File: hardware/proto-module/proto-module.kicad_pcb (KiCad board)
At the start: 2 copper layers, 80.4 x 50 mm, 4 parts, among them J1 Conn_01x30, U1 02x15_PIN_HEADER_SOCKET

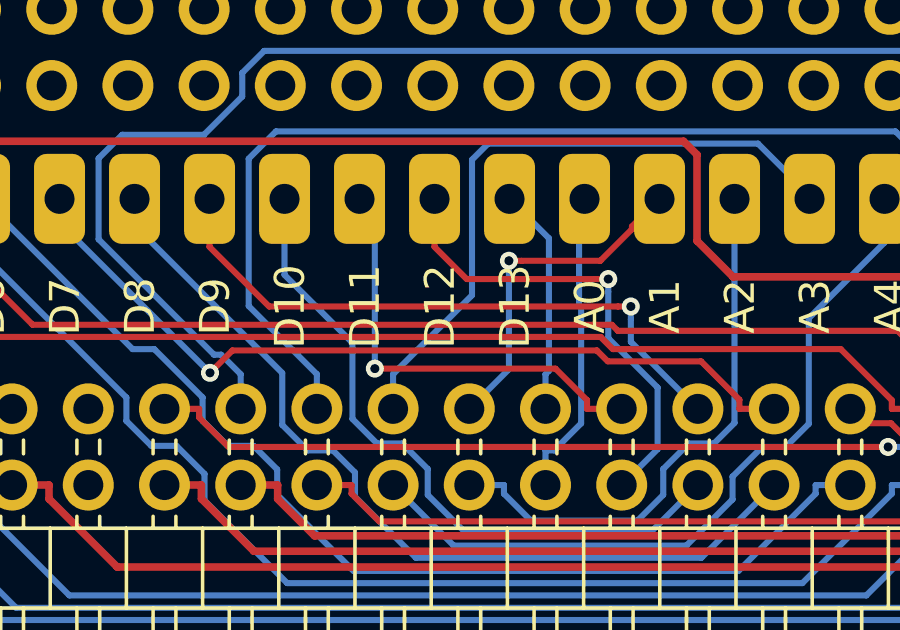
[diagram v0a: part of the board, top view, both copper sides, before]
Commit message: [hw] Make Proto Module production ready
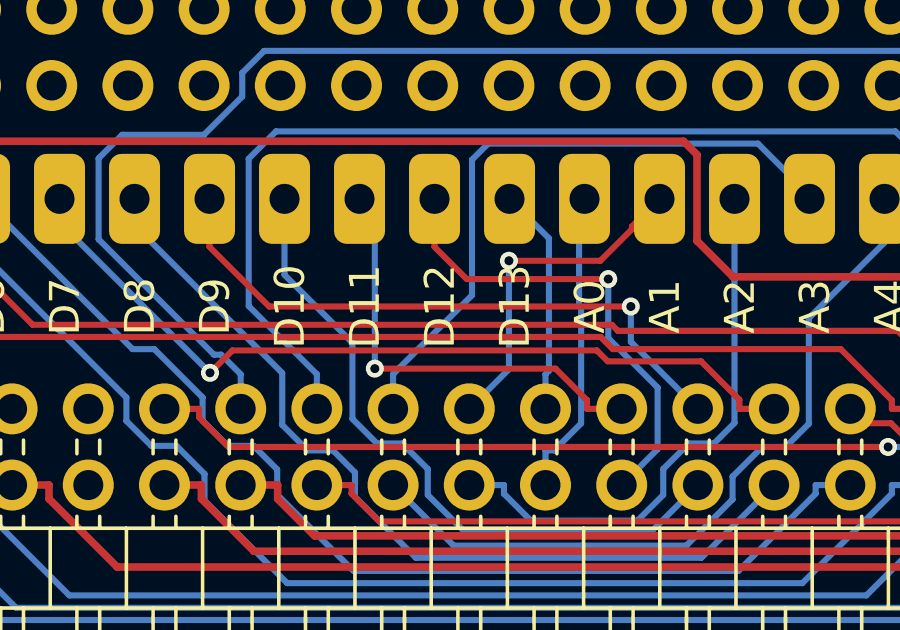
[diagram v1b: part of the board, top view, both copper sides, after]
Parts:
- moved G*** 0.69 mm to (164.9, 143.5)
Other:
- board text added: "Proto Module v0.1 : Designed by Aravinth www.arabeat.aravinth.info"
- board text removed: "Proto Module : Designed by Aravinth www.arabeat.aravinth.info"

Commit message: [hw] Make Proto Module production ready
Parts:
- moved G*** 0.31 mm to (165.1, 143.7)
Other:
- board text added: "PROTO Module v0.1 : Designed by Aravinth www.arabeat.aravinth.info"
- board text removed: "Proto Module v0.1 : Designed by Aravinth www.arabeat.aravinth.info"
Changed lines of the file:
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@@
   )
   (module ARABEAT:CASSETTE-LOGO (layer B.Cu)
-    (at 164.8714 143.4846 180)
+    (at 165.1 143.6878 180)
     (fp_text reference G*** (at 0 0 180) (layer B.SilkS) hide
       (effects (font (size 1.524 1.524) (thickness 0.3)) (justify mirror))
@@
       (xy -6.934787 4.864965) (xy -6.14133 4.98258) (xy -5.408771 4.954712)) (layer B.SilkS) (width 0.01))
   )
-  (gr_text "Proto Module v0.1 : Designed by Aravinth\nwww.arabeat.aravinth.info\n" (at 124.9172 145.3134) (layer B.SilkS)
+  (gr_text "PROTO Module v0.1 : Designed by Aravinth\nwww.arabeat.aravinth.info\n" (at 125.3998 145.2626) (layer B.SilkS)
     (effects (font (size 1.5 1.5) (thickness 0.3)) (justify mirror))
   )
